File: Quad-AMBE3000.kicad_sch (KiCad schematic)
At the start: 5 parts, among them J1 USB_C_Receptacle_USB2.0_14P, U1 FT4232H

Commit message: UARTS & PSU finished. Just AMBE-3000R stuff to go
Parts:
- removed C1: 100n, symbol Device:C_Small
- removed J1: USB_C_Receptacle_USB2.0_14P, symbol Connector:USB_C_Receptacle_USB2.0_14P
- removed R1, R2: 5k1, symbol Device:R_Small
- removed U1: FT4232H, symbol Interface_USB:FT4232H
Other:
- added sheet Power Supplies & Sequencing (psu.kicad_sch)
- added sheet USB & UART Interface (uarts.kicad_sch)

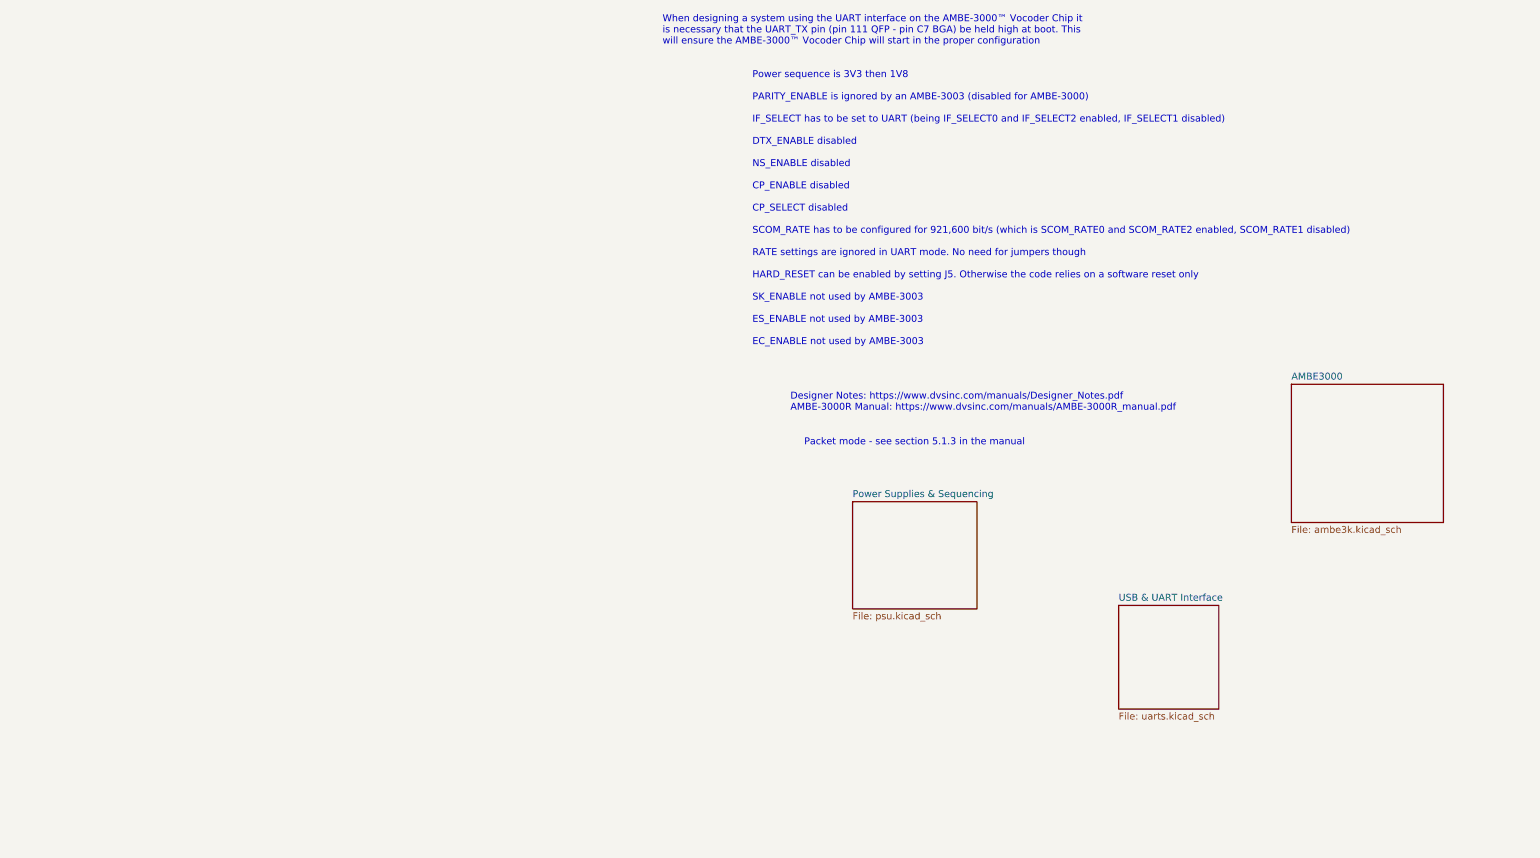
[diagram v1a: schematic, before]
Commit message: Added the AMBE-3000F
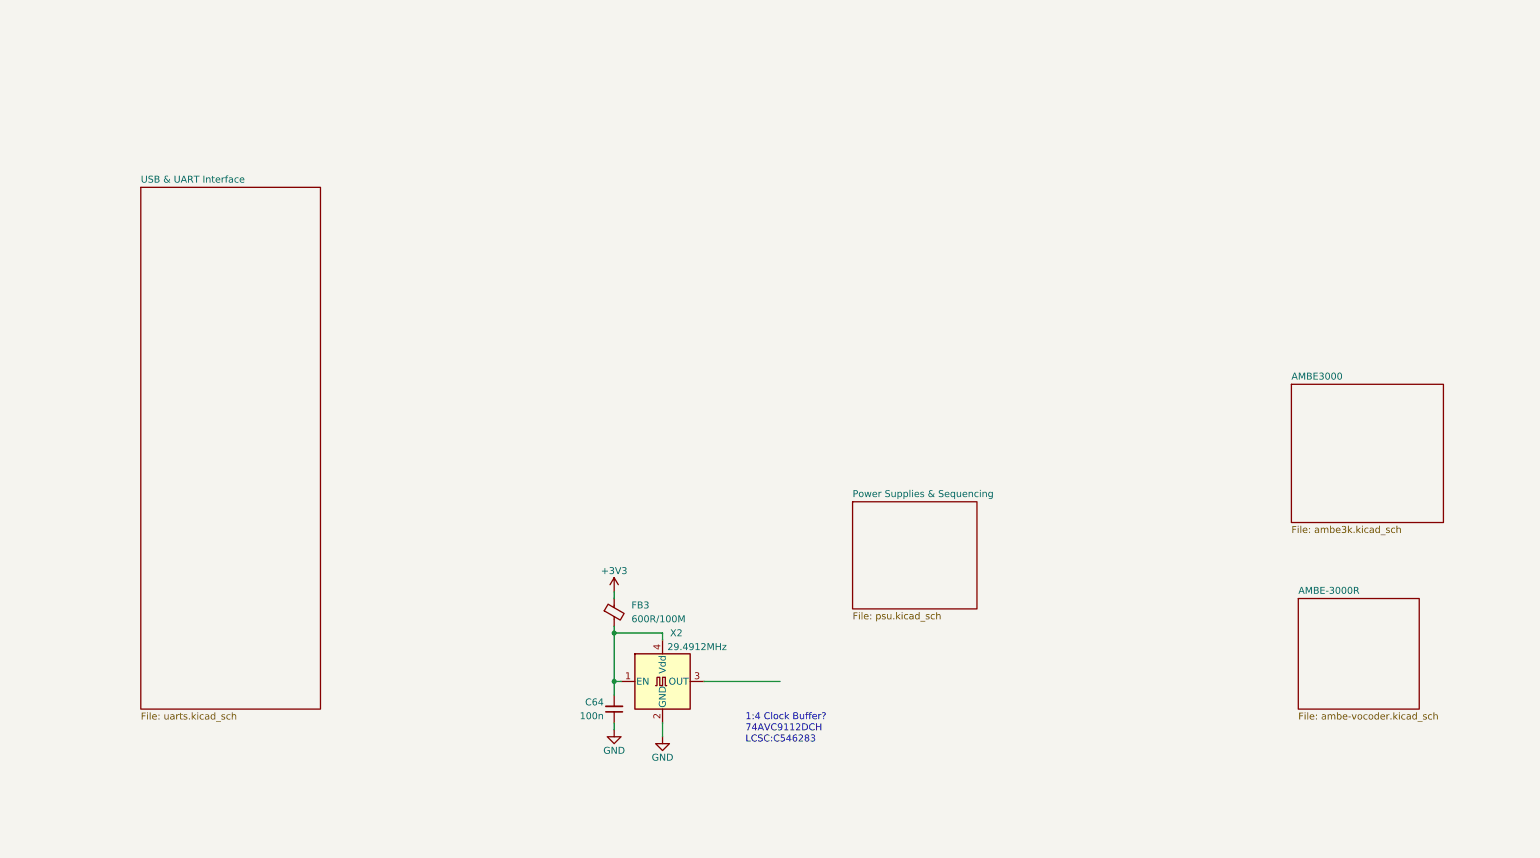
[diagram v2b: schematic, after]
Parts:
- added C64: 100n, symbol Device:C_Small
- added FB3: 600R/100M, symbol Device:FerriteBead_Small
- added X2: 29.4912MHz, Oscillator:Oscillator_SMD_Abracon_ASV-4Pin_7.0x5.1mm, symbol Oscillator:ASV-xxxMHz
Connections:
- new net: C64.2, FB3.2, X2.1 (EN), X2.4 (Vdd)
- new net +3V3: FB3.1
- new net GND: C64.1, X2.2 (GND)
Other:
- added sheet AMBE-3000R (ambe-vocoder.kicad_sch)
- note added: "1:4 Clock Buffer? 74AVC9112DCH LCSC:C546283"
- note removed: "Designer Notes: https://www.dvsinc.com/manuals/Designer_Notes.pdf AMBE-3000R Manual: https://www.dvsinc.com/manuals/AMBE-3000R_manual.pdf"
- note removed: "Packet mode - see section 5.1.3 in the manual"
- note removed: "Power sequence is 3V3 then 1V8 PARITY_ENABLE is ignored by an AMBE-3003 (disabled for AMBE-3000) IF_SELECT has to be set to UART (being IF_SELECT0 and IF_SELECT2 enabled, IF_SELECT1 disabled) DTX_ENABLE disabled NS_ENABLE disabled CP_ENABLE disabled CP_SELECT disabled SCOM_RATE has to be configured for 921,600 bit/s (which is SCOM_RATE0 and SCOM_RATE2 enabled, SCOM_RATE1 disabled) RATE settings a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"
- note removed: "When designing a system using the UART interface on the AMBE-3000™ Vocoder Chip it is necessary that the UART_TX pin (pin 111 QFP - pin C7 BGA) be held high at boot. This will ensure the AMBE-3000™ Vocoder Chip will start in the proper configuration"
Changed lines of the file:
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@@
 (kicad_sch (version 20230121) (generator eeschema)
   (paper "A4")
-  (text "When designing a system using the UART interface on the AMBE-3000™ Vocoder Chip it\nis necessary that the UART_TX pin (pin 111 QFP - pin C7 BGA) be held high at boot. This\nwill ensure the AMBE-3000™ Vocoder Chip will start in the proper configuration"
-    (at 132.08 22.86 0)
+  (junction (at 123.19 139.7) (diameter 0) (color 0 0 0 0)
+  )
+  (junction (at 123.19 130.81) (diameter 0) (color 0 0 0 0)
+  )
+  (wire (pts (xy 132.08 132.08) (xy 132.08 130.81))
+    (stroke (width 0) (type default))
+  )
+  (wire (pts (xy 139.7 139.7) (xy 153.67 139.7))
+    (stroke (width 0) (type default))
+  )
+  (wire (pts (xy 123.19 130.81) (xy 123.19 139.7))
+    (stroke (width 0) (type default))
+  )
+  (wire (pts (xy 123.19 129.54) (xy 123.19 130.81))
+    (stroke (width 0) (type default))
+  )
+  (wire (pts (xy 123.19 123.19) (xy 123.19 124.46))
+    (stroke (width 0) (type default))
+  )
+  (wire (pts (xy 132.08 130.81) (xy 123.19 130.81))
+    (stroke (width 0) (type default))
+  )
+  (wire (pts (xy 123.19 139.7) (xy 123.19 142.24))
+    (stroke (width 0) (type default))
+  )
+  (wire (pts (xy 132.08 147.32) (xy 132.08 149.86))
+    (stroke (width 0) (type default))
+  )
+  (wire (pts (xy 123.19 147.32) (xy 123.19 148.59))
+    (stroke (width 0) (type default))
+  )
+  (wire (pts (xy 123.19 139.7) (xy 124.46 139.7))
+    (stroke (width 0) (type default))
+  )
+  (text "1:4 Clock Buffer?\n74AVC9112DCH\nLCSC:C546283" (at 147.32 151.13 0)
     (effects (font (size 1.27 1.27)) (justify left bottom))
   )
-  (text "Designer Notes: https://www.dvsinc.com/manuals/Designer_Notes.pdf\nAMBE-3000R Manual: https://www.dvsinc.com/manuals/AMBE-3000R_manual.pdf"
-    (at 155.575 90.17 0)
-    (effects (font (size 1.27 1.27)) (justify left bottom))
-  )
-  (text "Power sequence is 3V3 then 1V8\n\nPARITY_ENABLE is ignored by an AMBE-3003 (disabled for AMBE-3000)\n\nIF_SELECT has to be set to UART (being IF_SELECT0 and IF_SELECT2 enabled, IF_SELECT1 disabled)\n\nDTX_ENABLE disabled\n\nNS_ENABLE disabled\n\nCP_ENABLE disabled\n\nCP_SELECT disabled\n\nSCOM_RATE has to be configured for 921,600 bit/s (which is SCOM_RATE0 and SCOM_RATE2 enabled, SCOM_RATE1 disabled)\n\nRATE settings are ignored in UART mode. No need for jumpers though\n\nHARD_RESET can be enabled by setting J5. Otherwise the code relies on a software reset only\n\nSK_ENABLE not used by AMBE-3003\n\nES_ENABLE not used by AMBE-3003\n\nEC_ENABLE not used by AMBE-3003"
-    (at 148.59 78.105 0)
-    (effects (font (size 1.27 1.27)) (justify left bottom))
-  )
-  (text "Packet mode - see section 5.1.3 in the manual" (at 158.115 96.52 0)
-    (effects (font (size 1.27 1.27)) (justify left bottom))
+  (symbol (lib_id "power:GND") (at 132.08 149.86 0) (mirror y) (unit 1)
+    (in_bom yes) (on_board yes) (dnp no)
+    (property "Reference" "#PWR0137" (at 132.08 156.21 0)
+      (effects (font (size 1.27 1.27)) hide)
+    )
+    (property "Value" "GND" (at 132.08 153.67 0)
+      (effects (font (size 1.27 1.27)))
+    )
+    (property "Footprint" "" (at 132.08 149.86 0)
+      (effects (font (size 1.27 1.27)) hide)
+    )
+    (property "Datasheet" "" (at 132.08 149.86 0)
+      (effects (font (size 1.27 1.27)) hide)
+    )
+    (pin "1")
+    (instances
+      (project "Quad-AMBE3000"
+        (path "/5724fa40-164f-4058-9cc8-ef80d9809dcd"
+          (reference "#PWR0137") (unit 1)
+        )
+      )
+    )
+  )
+  (symbol (lib_id "Device:FerriteBead_Small") (at 123.19 127 0) (unit 1)
+    (in_bom yes) (on_board yes) (dnp no)
+    (property "Reference" "FB3" (at 126.365 125.6919 0)
+      (effects (font (size 1.27 1.27)) (justify left))
+    )
+    (property "Value" "600R/100M" (at 126.365 128.2319 0)
+      (effects (font (size 1.27 1.27)) (justify left))
+    )
+    (property "Footprint" "" (at 121.412 127 90)
+      (effects (font (size 1.27 1.27)) hide)
+    )
+    (property "Datasheet" "~" (at 123.19 127 0)
+      (effects (font (size 1.27 1.27)) hide)
+    )
+    (pin "2")
+    (pin "1")
+    (instances
+      (project "Quad-AMBE3000"
+        (path "/5724fa40-164f-4058-9cc8-ef80d9809dcd"
+          (reference "FB3") (unit 1)
+        )
+      )
+    )
+  )
+  (symbol (lib_id "power:+3V3") (at 123.19 123.19 0) (unit 1)
+    (in_bom yes) (on_board yes) (dnp no)
+    (property "Reference" "#PWR0141" (at 123.19 127 0)
+      (effects (font (size 1.27 1.27)) hide)
+    )
+    (property "Value" "+3V3" (at 123.19 119.38 0)
+      (effects (font (size 1.27 1.27)))
+    )
+    (property "Footprint" "" (at 123.19 123.19 0)
+      (effects (font (size 1.27 1.27)) hide)
+    )
+    (property "Datasheet" "" (at 123.19 123.19 0)
+      (effects (font (size 1.27 1.27)) hide)
+    )
+    (pin "1")
+    (instances
+      (project "Quad-AMBE3000"
+        (path "/5724fa40-164f-4058-9cc8-ef80d9809dcd"
+          (reference "#PWR0141") (unit 1)
+        )
+      )
+    )
+  )
+  (symbol (lib_id "power:GND") (at 123.19 148.59 0) (unit 1)
+    (in_bom yes) (on_board yes) (dnp no)
+    (property "Reference" "#PWR0140" (at 123.19 154.94 0)
+      (effects (font (size 1.27 1.27)) hide)
+    )
+    (property "Value" "GND" (at 123.19 152.4 0)
+      (effects (font (size 1.27 1.27)))
+    )
+    (property "Footprint" "" (at 123.19 148.59 0)
+      (effects (font (size 1.27 1.27)) hide)
+    )
+    (property "Datasheet" "" (at 123.19 148.59 0)
+      (effects (font (size 1.27 1.27)) hide)
+    )
+    (pin "1")
+    (instances
+      (project "Quad-AMBE3000"
+        (path "/5724fa40-164f-4058-9cc8-ef80d9809dcd"
+          (reference "#PWR0140") (unit 1)
+        )
+      )
+    )
+  )
+  (symbol (lib_id "Oscillator:ASV-xxxMHz") (at 132.08 139.7 0) (unit 1)
+    (in_bom yes) (on_board yes) (dnp no)
+    (property "Reference" "X2" (at 134.62 130.81 0)
+      (effects (font (size 1.27 1.27)))
+    )
+    (property "Value" "29.4912MHz" (at 138.43 133.35 0)
+      (effects (font (size 1.27 1.27)))
+    )
+    (property "Footprint" "Oscillator:Oscillator_SMD_Abracon_ASV-4Pin_7.0x5.1mm" (at 149.86 148.59 0)
+      (effects (font (size 1.27 1.27)) hide)
+    )
+    (property "Datasheet" "https://datasheet.lcsc.com/lcsc/2110101030_Shenzhen-SCTF-Elec-SX7M29-4912M20F30TNN_C2901492.pdf" (at 129.54 139.7 0)
+      (effects (font (size 1.27 1.27)) hide)
+    )
+    (property "LCSC" "C2901492" (at 132.08 139.7 0)
+      (effects (font (size 1.27 1.27)) hide)
+    )
+    (pin "4")
+    (pin "2")
+    (pin "1")
+    (pin "3")
+    (instances
+      (project "Quad-AMBE3000"
+        (path "/5724fa40-164f-4058-9cc8-ef80d9809dcd"
+          (reference "X2") (unit 1)
+        )
+      )
+    )
+  )
+  (symbol (lib_id "Device:C_Small") (at 123.19 144.78 0) (mirror x) (unit 1)
+    (in_bom yes) (on_board yes) (dnp no)
+    (property "Reference" "C64" (at 121.285 143.51 0)
+      (effects (font (size 1.27 1.27)) (justify right))
+    )
+    (property "Value" "100n" (at 121.285 146.05 0)
+      (effects (font (size 1.27 1.27)) (justify right))
+    )
+    (property "Footprint" "" (at 123.19 144.78 0)
+      (effects (font (size 1.27 1.27)) hide)
+    )
+    (property "Datasheet" "~" (at 123.19 144.78 0)
+      (effects (font (size 1.27 1.27)) hide)
+    )
+    (pin "1")
+    (pin "2")
+    (instances
+      (project "Quad-AMBE3000"
+        (path "/5724fa40-164f-4058-9cc8-ef80d9809dcd"
+          (reference "C64") (unit 1)
+        )
+      )
+    )
+  )
+  (sheet (at 248.92 124.46) (size 22.225 20.32) (fields_autoplaced)
+    (stroke (width 0.1524) (type solid))
+    (fill (color 0 0 0 0.0000))
+    (property "Sheetname" "AMBE-3000R" (at 248.92 123.7484 0)
+      (effects (font (size 1.27 1.27)) (justify left bottom))
+    )
+    (property "Sheetfile" "ambe-vocoder.kicad_sch" (at 248.92 145.3646 0)
+      (effects (font (size 1.27 1.27)) (justify left top))
+    )
+    (instances
+      (project "Quad-AMBE3000"
+        (path "/5724fa40-164f-4058-9cc8-ef80d9809dcd" (page "5"))
+      )
+    )
   )
   (sheet (at 247.65 85.09) (size 27.94 25.4) (fields_autoplaced)
@@
     )
   )
-  (sheet (at 215.9 125.73) (size 18.415 19.05) (fields_autoplaced)
-    (stroke (width 0.1524) (type solid))
-    (fill (color 0 0 0 0.0000))
-    (property "Sheetname" "USB & UART Interface" (at 215.9 125.0184 0)
-      (effects (font (size 1.27 1.27)) (justify left bottom))
-    )
-    (property "Sheetfile" "uarts.kicad_sch" (at 215.9 145.3646 0)
-      (effects (font (size 1.27 1.27)) (justify left top))
-    )
+  (sheet (at 36.195 48.895) (size 33.02 95.885) (fields_autoplaced)
+    (stroke (width 0.1524) (type solid))
+    (fill (color 0 0 0 0.0000))
+    (property "Sheetname" "USB & UART Interface" (at 36.195 48.1834 0)
+      (effects (font (size 1.27 1.27)) (justify left bottom))
+    )
+    (property "Sheetfile" "uarts.kicad_sch" (at 36.195 145.3646 0)
+      (effects (font (size 1.27 1.27)) (justify left top))
+    )

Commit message: Schematic V1 done
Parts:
- added C2: 100n, Capacitor_SMD:C_0603_1608Metric, symbol Device:C_Small
- added R1, R2, R3, R4, R5: 33R, Resistor_SMD:R_0603_1608Metric, symbol Device:R_Small
- added U1: 74AVC9112DCH, Package_SO:VSSOP-8_2.4x2.1mm_P0.5mm, symbol 74AVC9112DCH:74AVC9112DCH
- C1: renamed from C64; footprint (none) -> Capacitor_SMD:C_0603_1608Metric
- FB1: renamed from FB3; footprint (none) -> Inductor_SMD:L_0805_2012Metric; LCSC (none) -> C1017
- renumbered X2 to X1
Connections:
- net +3V3: now also FB1.2; no longer FB1.1
- net GND: now also C2.1, U1.4 (GND)
- net at C1.2, X1.1 (EN), X1.4 (Vdd): now also FB1.1, C2.2, U1.1 (VCC), U1.3 (~{OE}); no longer FB1.2
- net at X1.3 (OUT): now also R1.1
- new net: R3.1, U1.6 (Y2)
- new net: R2.1, U1.5 (Y1)
- new net: R1.2, U1.2 (A)
- new net: R4.1, U1.7 (Y3)
- new net: R5.1, U1.8 (Y4)
- new net CLK_A: R2.2
- new net CLK_B: R3.2
- new net CLK_C: R4.2
- new net CLK_D: R5.2
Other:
- sheet AMBE-3000R renamed AMBE-3000R-A
- removed sheet AMBE3000
- added sheet AMBE-3000R-B (ambe-vocoder.kicad_sch)
- added sheet AMBE-3000R-C (ambe-vocoder.kicad_sch)
- added sheet AMBE-3000R-D (ambe-vocoder.kicad_sch)
- sheet AMBE-3000R-A ports: added AMBE_CLK_IN, AMBE_UART_DTR, AMBE_UART_RTS, AMBE_UART_RX, AMBE_UART_TX; removed none
- sheet USB & UART Interface ports: added FTDI_A_CTS, FTDI_A_DTR, FTDI_A_RXD, FTDI_A_TXD, FTDI_B_CTS, FTDI_B_DTR, FTDI_B_RXD, FTDI_B_TXD, FTDI_C_CTS, FTDI_C_DTR, FTDI_C_RXD, FTDI_C_TXD, FTDI_D_CTS, FTDI_D_DTR, FTDI_D_RXD, FTDI_D_TXD; removed none
- note added: "Clock & Fanout"
- note added: "For digital voice decoding & transcoding systems, WebSDR receivers, etc."
- note added: "George Smart, M1GEO. https://github.com/m1geo/Quad-AMBE3000"
- note added: "Quad AMBE-3000R Board"
- note removed: "1:4 Clock Buffer? 74AVC9112DCH LCSC:C546283"
- company: (none) -> M1GEO & G8OCV
- title: (none) -> Quad AMBE-3000R Board
- moved on the sheet: C1, FB1, X1
